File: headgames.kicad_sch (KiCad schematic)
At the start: 48 parts, among them J1 9V BATTERY IN, J2 ELECTRODES, U1 LM358N INVENTORY, U2 LM324N INVENTORY, U3 LM386

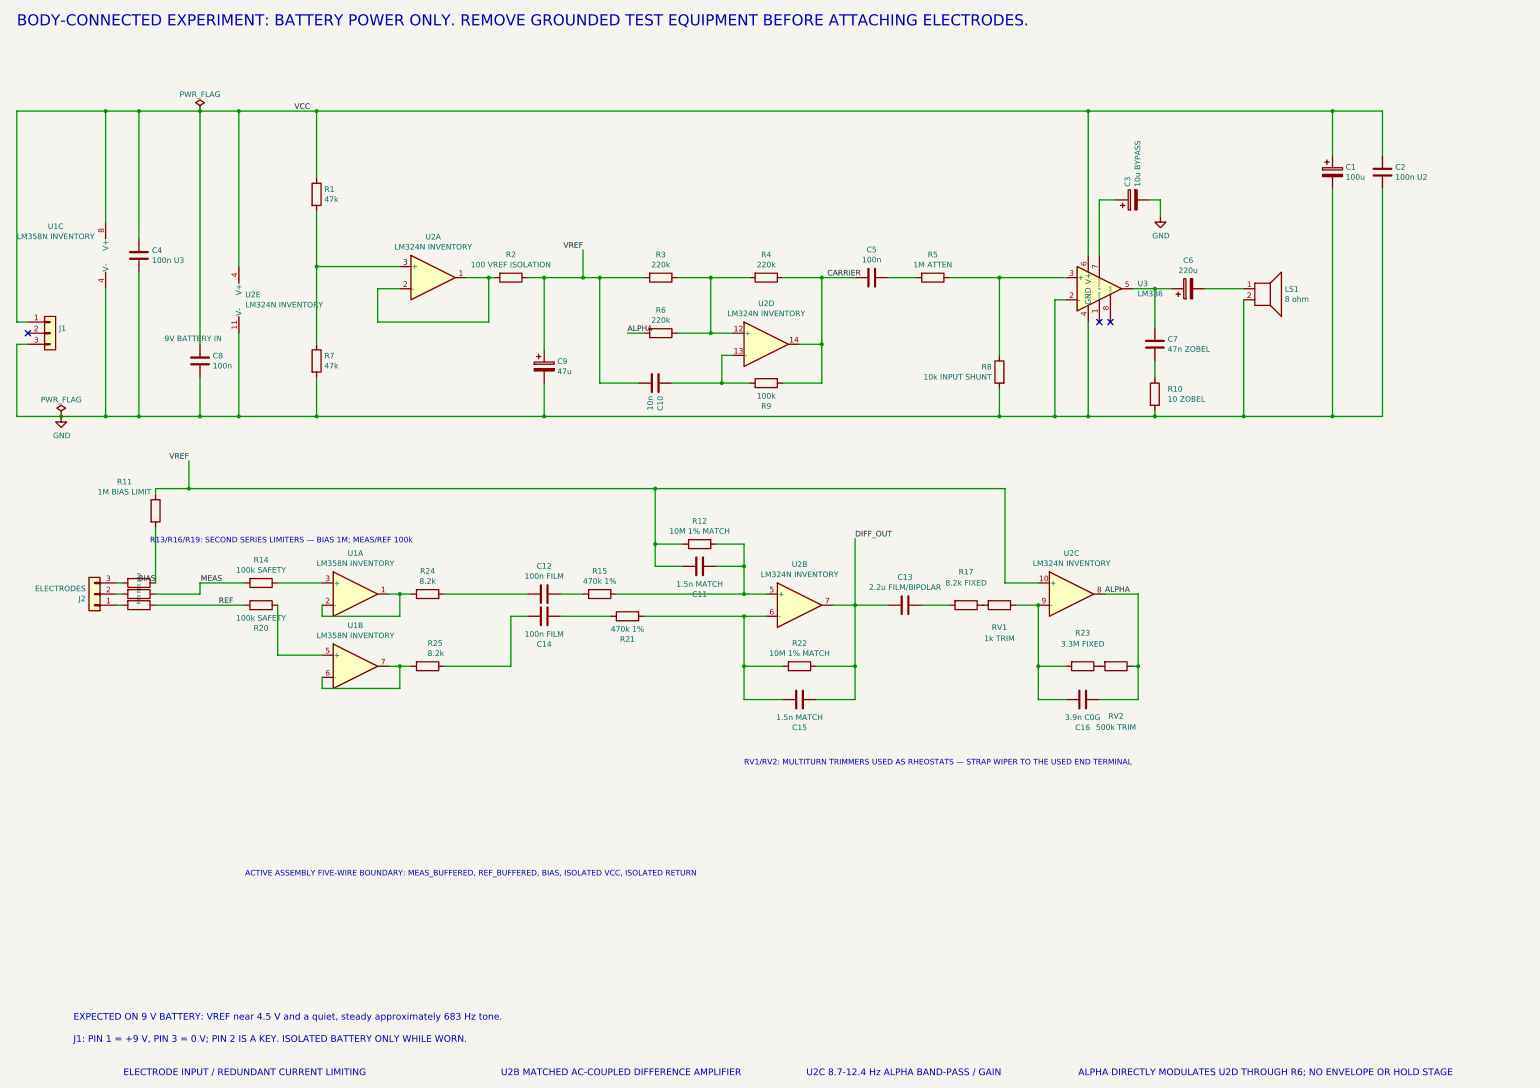
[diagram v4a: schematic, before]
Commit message: Maximize pre-bench simulation evidence and standardize on KiCad 9
Restore the authoritative schematic to KiCad 9 format as explicitly required. Preserve the explicit MEAS/REF active-buffer paths while splitting both LM358 follower outputs at literal shared endpoints and routing the acquisition returns without overlapping collinear wires. KiCad 9.0.9 now loads the file natively, exports its netlist, and reports zero ERC violations.

Remove the prior 100 ohm analytical cable-margin assertion because it neither represented schematic R24/R25 nor computed a valid return ratio. Add a KiCad-backed command that exercises the actual 8.2 kohm ±5 percent and 150/250 pF TI transient corners. Those four nominal macro-model cases pass with zero measured overshoot and 8.9 microsecond worst settling. Keep phase margin explicitly unresolved: valid loop-break fixtures fail to converge in the available TI macro-model, and TI supplies no process/temperature corner set.

Expand selected-path physical spreads across electrode interface parameters, input capacitance, buffer bandwidth/noise, cable capacitance, safety resistors, matched acquisition pairs, alpha parts, oscillator rails, supply/VREF, conservative LM386 datasheet bounds, output network, and speaker resistance. Preserve intended correlation for the measured R15/R21 and matched R12/R22 pairs while independently moving unrelated leaves.

Parameterize the nonlinear behavioral endpoint with oscillator swing, LM386 gain/input resistance/bandwidth/conservative 250-325 mW clipping power, and speaker resistance instead of hard-coded constants. Add a deterministic selected-path campaign command with exact build and phase accounting, endpoint current, margin, clipping, and latching reports.

Measured result: the nominal 16-phase wet/alpha run still fails at 0.24 percent alpha/carrier versus the 1 percent gate. A repeated deterministic 17-build by 16-phase campaign executed all 272 complete speaker-current cases; all 17 builds failed alph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
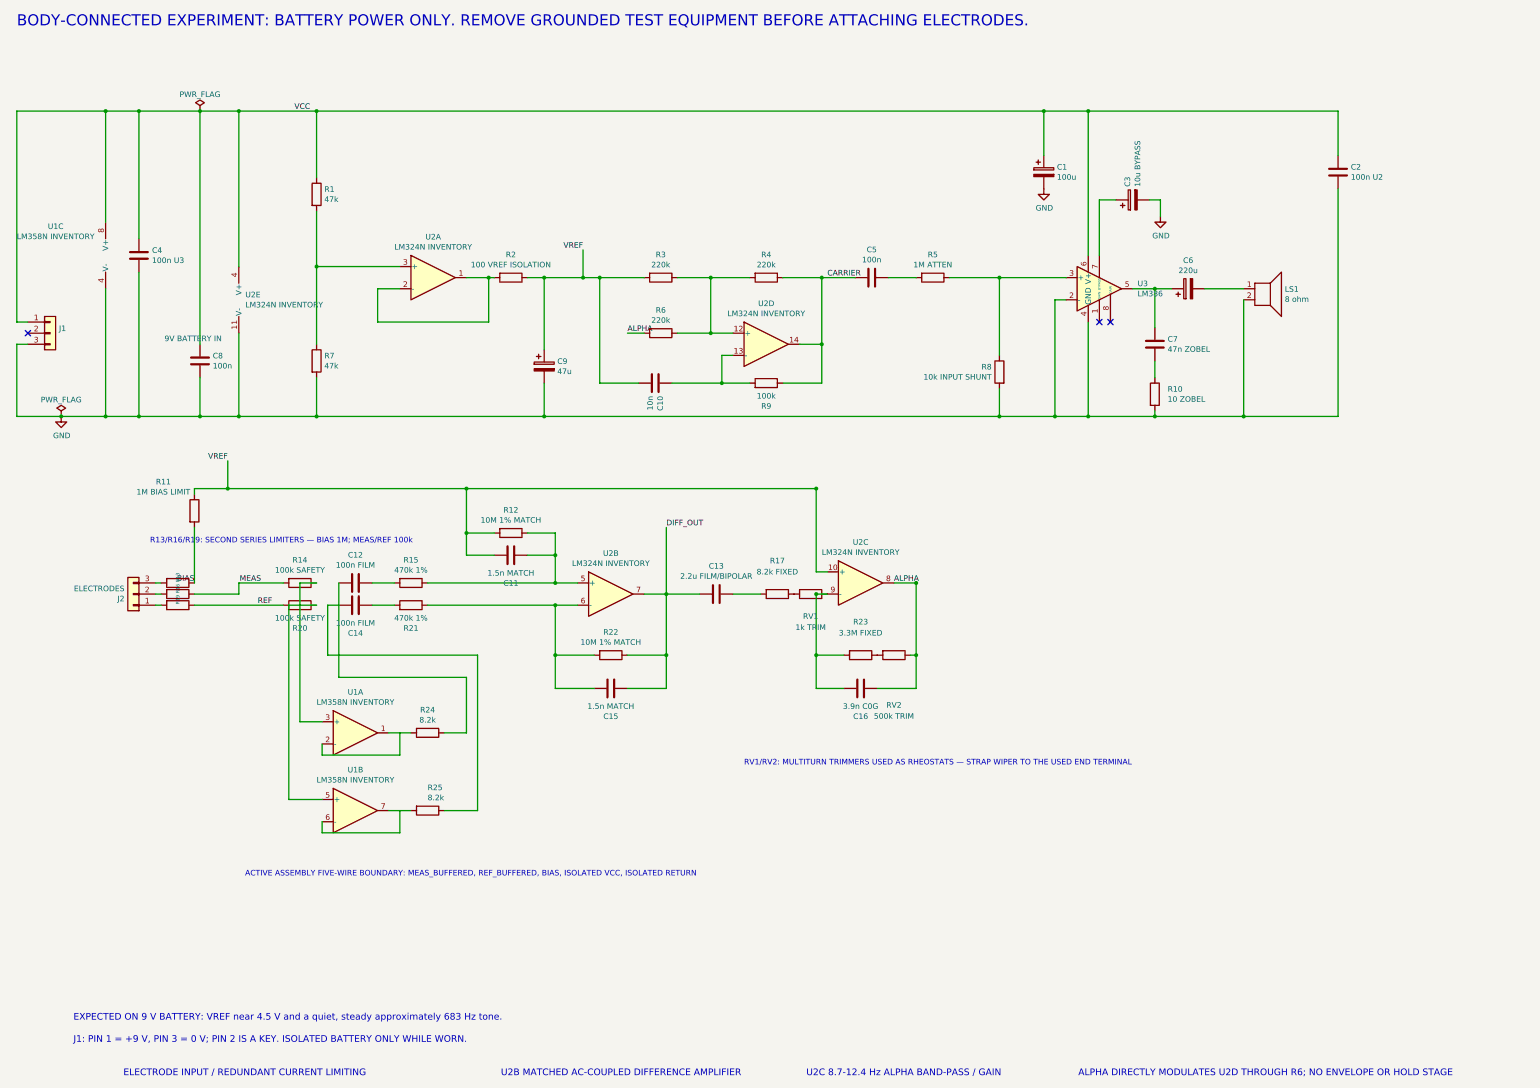
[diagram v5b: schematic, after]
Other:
- moved on the sheet: C1, C11, C12, C13, C14, C15, C16, C2, J2, R11, R12, R13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

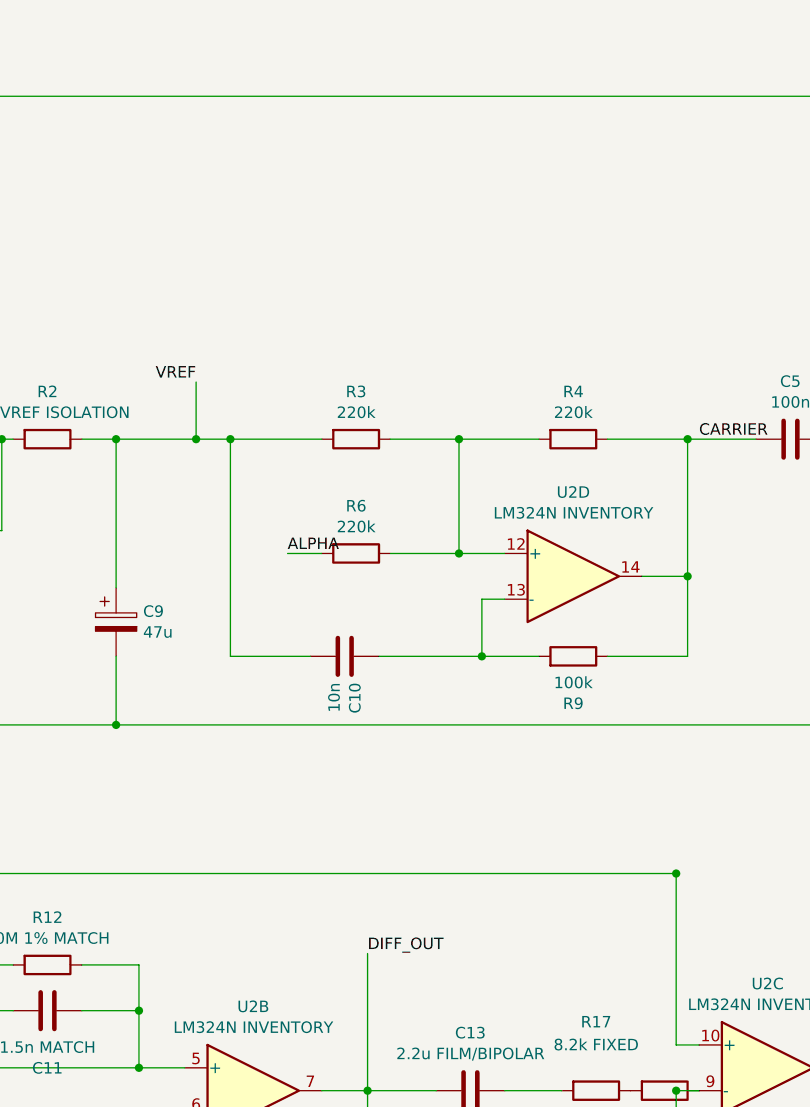
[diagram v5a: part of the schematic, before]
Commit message: Add bounded oscillator modulation rheostat
Replace the fixed 220 kΩ ALPHA-to-U2D coupling resistor with a 68 kΩ R6 floor in series with a 250 kΩ RV3 external linear rheostat. The fixed resistor prevents a zero-resistance control setting while the rheostat exposes a practical 68–318 kΩ adjustment range for carrier modulation strength.

Represent RV3 using the schematic's established two-terminal external-rheostat convention and explicitly instruct builders to strap the wiper to the R6 end. Preserve the drawn signal-path continuity by placing RV3 directly in the former R6-to-U2D wire segment.

Teach the behavioral model to derive its midpoint coupling resistance from both physical schematic parts and move the two leaves independently during sampled builds. Extend native topology checks to prove the R6/RV3 series net, U2D termination, component values, and complete adjustment bounds.

Update the architectural invariant and verify the checkpoint with the root manage.py regression suite, including KiCad netlist export and ERC, plus git diff whitespace validation.
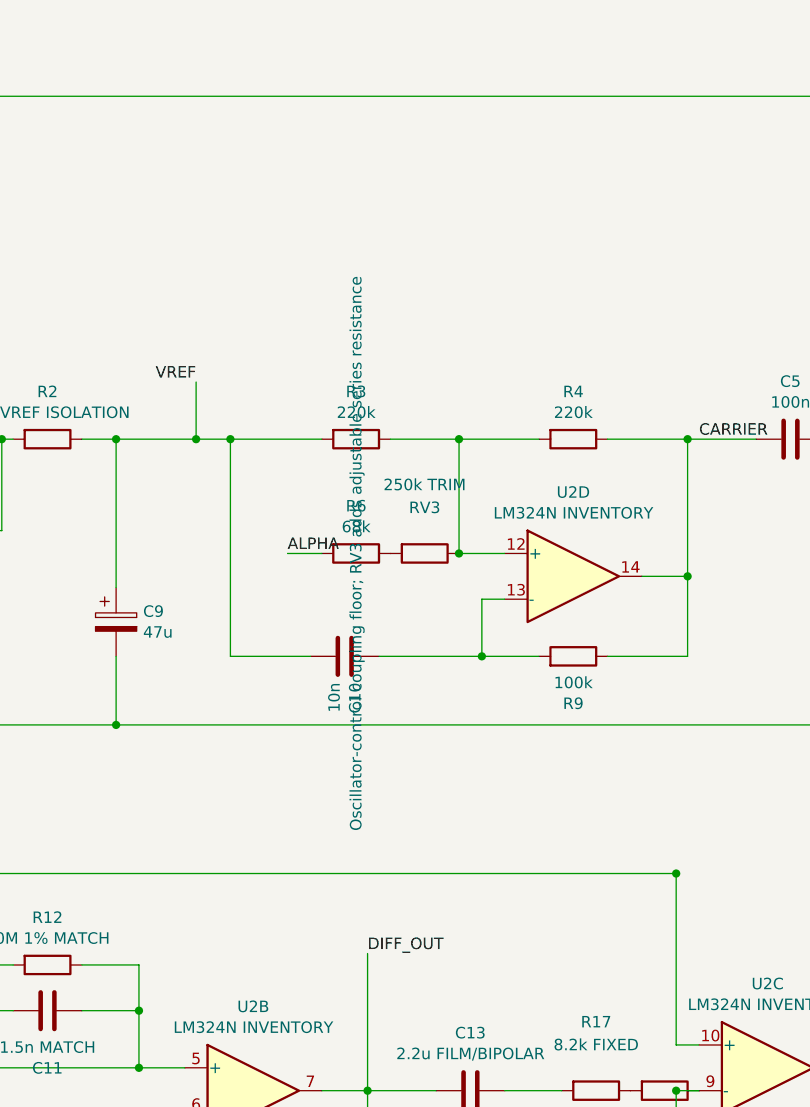
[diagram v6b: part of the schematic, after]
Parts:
- added RV3: 250k TRIM, symbol Device:R
- R6: value 220k -> 68k
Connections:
- net at R3.1, R4.2, U2.12 (+): now also RV3.1; no longer R6.1
- new net: R6.1, RV3.2
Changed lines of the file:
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@@
-	(wire
-		(pts
-			(xy 168.91 88.9) (xy 176.53 88.9)
-		)
-		(stroke
-			(width 0)
-			(type default)
-		)
-	)
 	(wire
 		(pts
@@
 	(symbol
 		(lib_id "Device:R")
+		(at 172.72 88.9 270)
+		(unit 1)
+		(exclude_from_sim no)
+		(in_bom yes)
+		(on_board yes)
+		(dnp no)
+		(property "Reference" "RV3"
+			(at 172.72 83.82 90)
+			(effects (font (size 1.27 1.27)))
+		)
+		(property "Value" "250k TRIM"
+			(at 172.72 81.28 90)
+			(effects (font (size 1.27 1.27)))
+		)
+		(property "Footprint" ""
+			(at 172.72 88.9 0)
+			(effects (font (size 1.27 1.27)) (hide yes))
+		)
+		(property "Datasheet" "~"
+			(at 172.72 88.9 0)
+			(effects (font (size 1.27 1.27)) (hide yes))
+		)
+		(property "Description" "External 250k linear potentiometer used as rheostat; strap wiper to the R6 end"
+			(at 172.72 88.9 0)
+			(effects (font (size 1.27 1.27)) (hide yes))
+		)
+		(pin "1")
+		(pin "2")
+		(instances
+			(project "headgames"
+				(path "/16bca6b0-2f64-4676-a185-d512cb0de7e5"
+					(reference "RV3")
+					(unit 1)
+				)
+			)
+		)
+	)
+	(symbol
+		(lib_id "Device:R")
 		(at 165.1 76.2 270)
 		(unit 1)
@@
 			)
 		)
-		(property "Value" "220k"
+		(property "Value" "68k"
 			(at 165.1 85.9536 90)
 			(effects
@@
 			)
 		)
-		(property "Description" ""
+		(property "Description" "Oscillator-control coupling floor; RV3 adds adjustable series resistance"
 			(at 165.1 88.9 0)
 			(effects

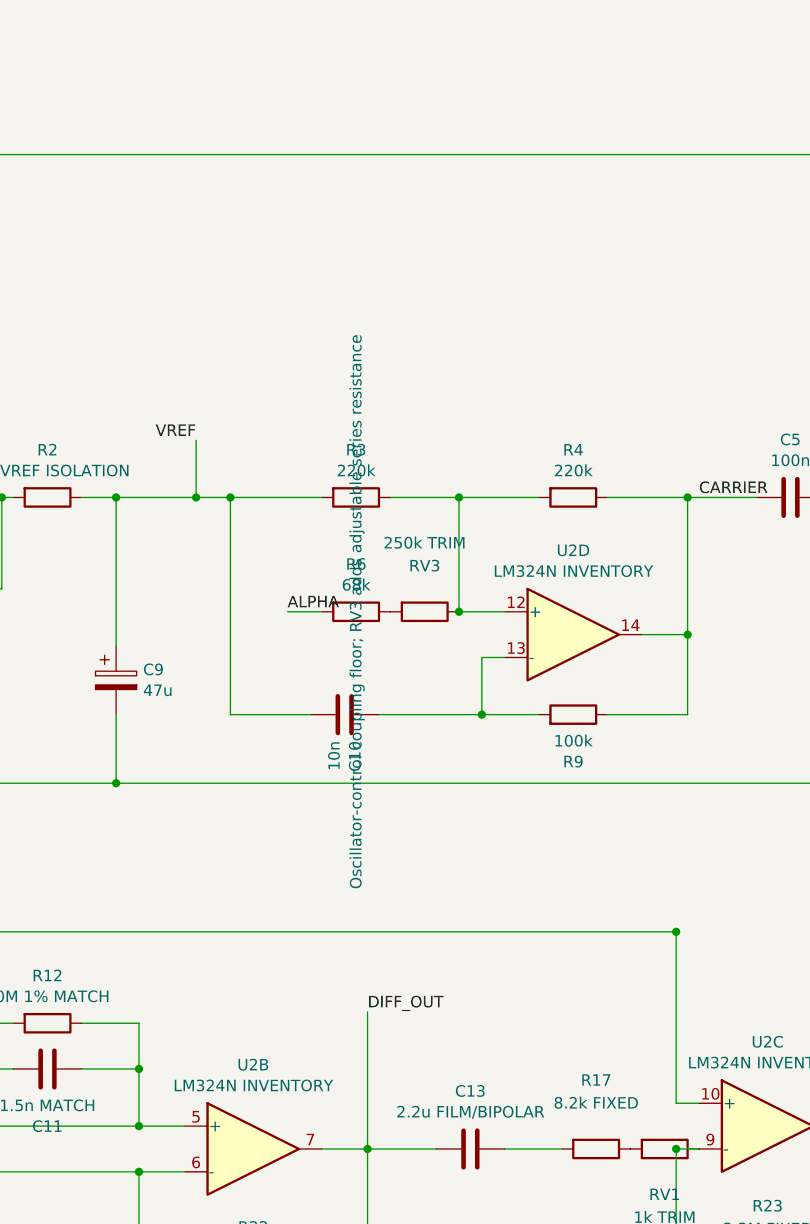
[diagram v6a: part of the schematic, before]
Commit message: Constrain oscillator rheostat to a useful local interval
Replace the overly broad 68–318 kΩ oscillator-control adjustment with a 180 kΩ fixed R6 and a 25 kΩ RV3, yielding a bounded 180–205 kΩ total resistance. This keeps the complete control-sensitivity span near 14 percent while making every setting approximately 7–22 percent stronger than the former fixed 220 kΩ coupling.

The small rheostat contribution also bounds sensitivity to its end-to-end tolerance: even a 10 percent RV3 error changes total series resistance by no more than about 1.2 percent. Preserve the fail-safe wiper strap and the explicit series topology.

Update schematic-derived model invariants and architectural guidance to the narrowed interval. Verify with the complete root regression suite, including KiCad netlist/ERC checks, and git diff whitespace validation.
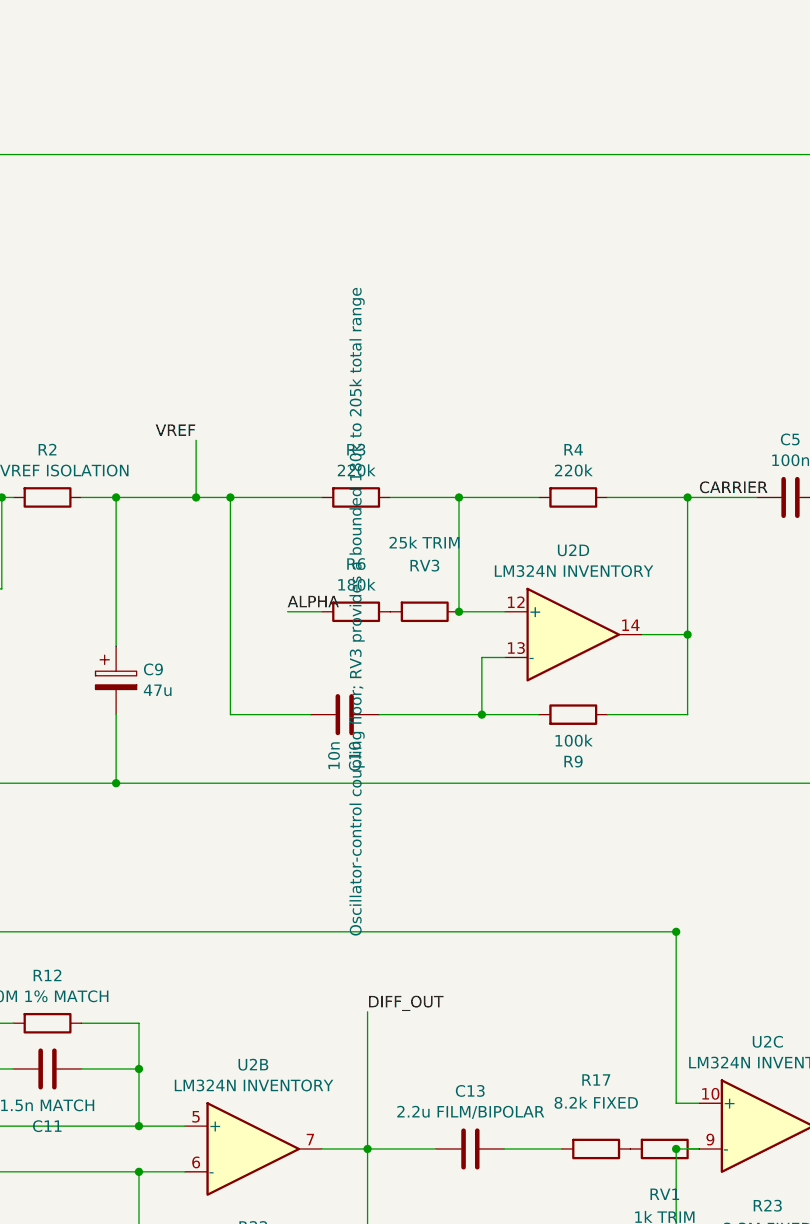
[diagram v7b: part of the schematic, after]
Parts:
- R6: value 68k -> 180k
- RV3: value 250k TRIM -> 25k TRIM
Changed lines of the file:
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@@
 			(effects (font (size 1.27 1.27)))
 		)
-		(property "Value" "250k TRIM"
+		(property "Value" "25k TRIM"
 			(at 172.72 81.28 90)
 			(effects (font (size 1.27 1.27)))
@@
 			(effects (font (size 1.27 1.27)) (hide yes))
 		)
-		(property "Description" "External 250k linear potentiometer used as rheostat; strap wiper to the R6 end"
+		(property "Description" "External 25k linear potentiometer used as rheostat; strap wiper to the R6 end"
 			(at 172.72 88.9 0)
 			(effects (font (size 1.27 1.27)) (hide yes))
@@
 			)
 		)
-		(property "Value" "68k"
+		(property "Value" "180k"
 			(at 165.1 85.9536 90)
 			(effects
@@
 			)
 		)
-		(property "Description" "Oscillator-control coupling floor; RV3 adds adjustable series resistance"
+		(property "Description" "Oscillator-control coupling floor; RV3 provides a bounded 180k to 205k total range"
 			(at 165.1 88.9 0)
 			(effects

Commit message: Show all oscillator rheostat pins explicitly
Replace RV3's two-terminal resistor abstraction with KiCad's stock three-pin R_Potentiometer symbol so the physical potentiometer terminals and wiper are visible in the authoritative schematic.

Connect terminal 1 toward the U2D oscillator input, terminal 3 toward the 180 kΩ R6 floor, and explicitly strap wiper terminal 2 to terminal 3. This preserves the intended fail-safe rheostat behavior: loss of wiper contact tends toward the full 25 kΩ track resistance instead of opening the modulation path.

Strengthen the native topology check to require R6, RV3 pin 3, and RV3 wiper pin 2 on exactly the same net while retaining the independent assertion that pin 1 reaches U2D. Verify the edited schematic with the root regression suite, KiCad netlist export, KiCad ERC, and git diff whitespace checks.
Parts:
- RV3: symbol Device:R -> Device:R_Potentiometer
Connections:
- net at R6.1, RV3.2: now also RV3.3
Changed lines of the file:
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@@
+	(wire
+		(pts
+			(xy 168.91 88.9) (xy 168.91 92.71)
+		)
+		(stroke
+			(width 0)
+			(type default)
+		)
+	)
+	(wire
+		(pts
+			(xy 168.91 92.71) (xy 172.72 92.71)
+		)
+		(stroke
+			(width 0)
+			(type default)
+		)
+	)
 	(wire
 		(pts
@@
 	)
 	(symbol
-		(lib_id "Device:R")
+		(lib_id "Device:R_Potentiometer")
 		(at 172.72 88.9 270)
 		(unit 1)
@@
 			(effects (font (size 1.27 1.27)) (hide yes))
 		)
-		(property "Description" "External 25k linear potentiometer used as rheostat; strap wiper to the R6 end"
+		(property "Description" "External 25k linear potentiometer used as rheostat; pins 2 and 3 strapped at the R6 end, pin 1 to U2D"
 			(at 172.72 88.9 0)
 			(effects (font (size 1.27 1.27)) (hide yes))
@@
 		(pin "1")
 		(pin "2")
+		(pin "3")
 		(instances
 			(project "headgames"
